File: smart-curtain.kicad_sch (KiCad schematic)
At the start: 71 parts, among them IC1 AS5040-ASST, IC2 ESP32-S3-MINI-1-N8, IC3 MPM3612GLQ-33-P, J1 USB4110-GF-A, J2 Limit, J3 Motor, J4 Qwiic 1, J5 Qwiic 2, SW1 Boot, SW2 Reset, U1 TMC2209-LA-T, U2 TPS25730DREFR

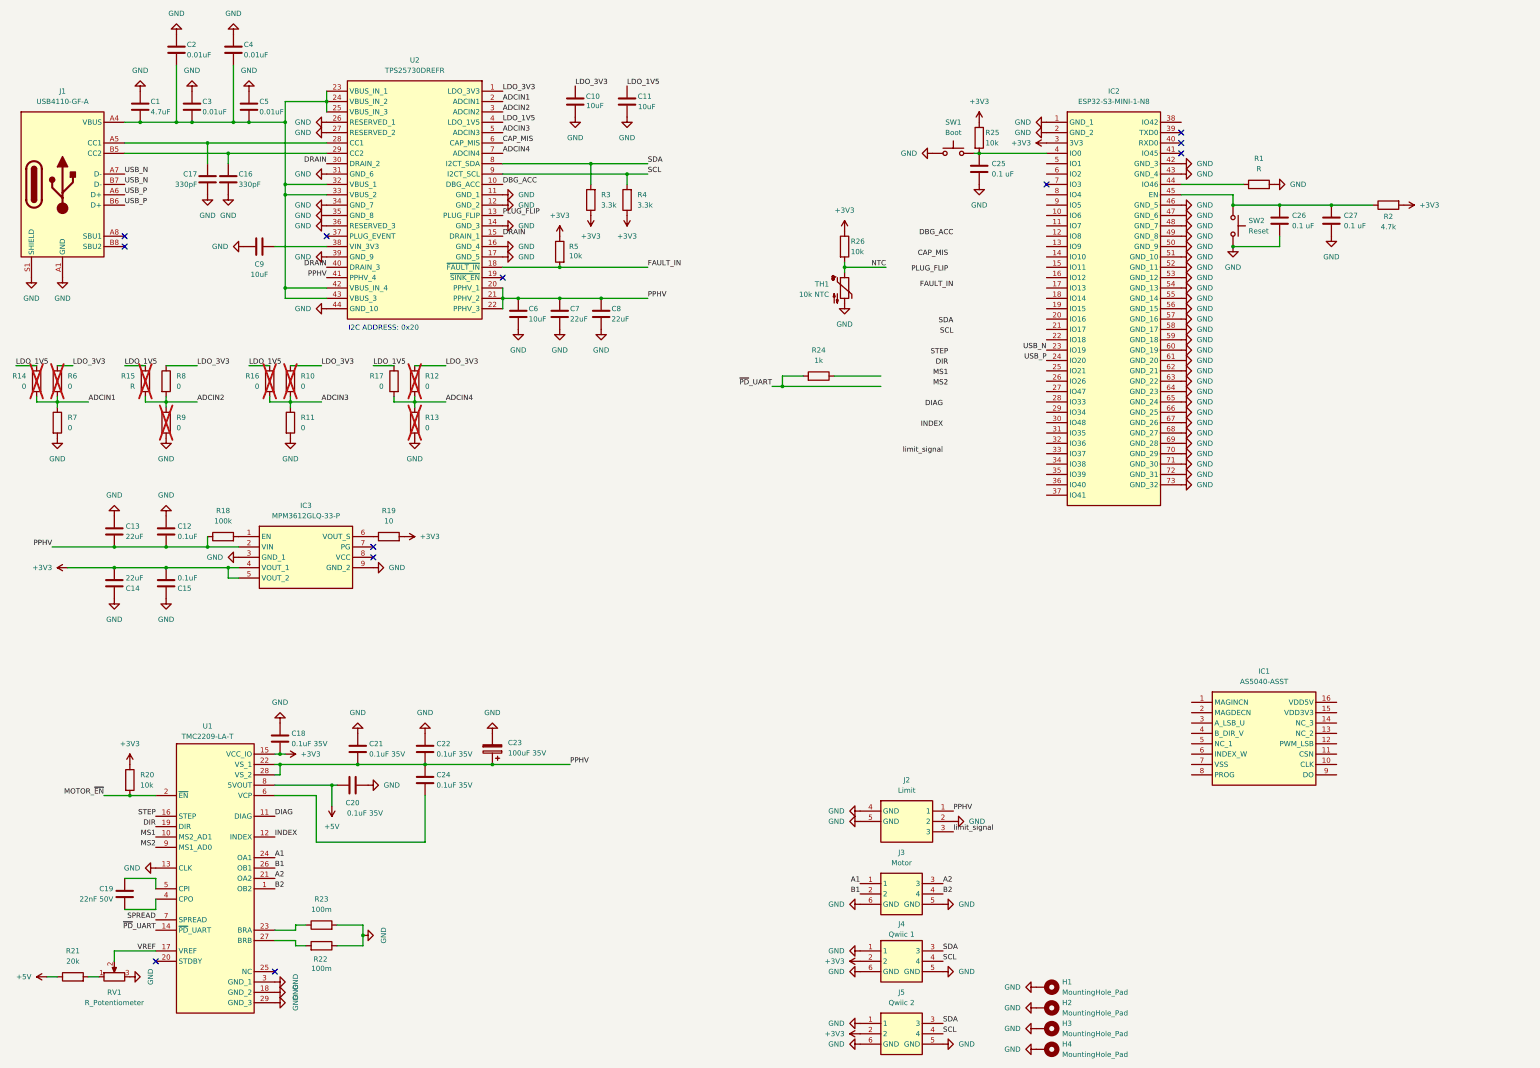
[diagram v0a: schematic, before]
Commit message: Update smart-curtain.kicad_sch
Connect labels to ESP pin`s
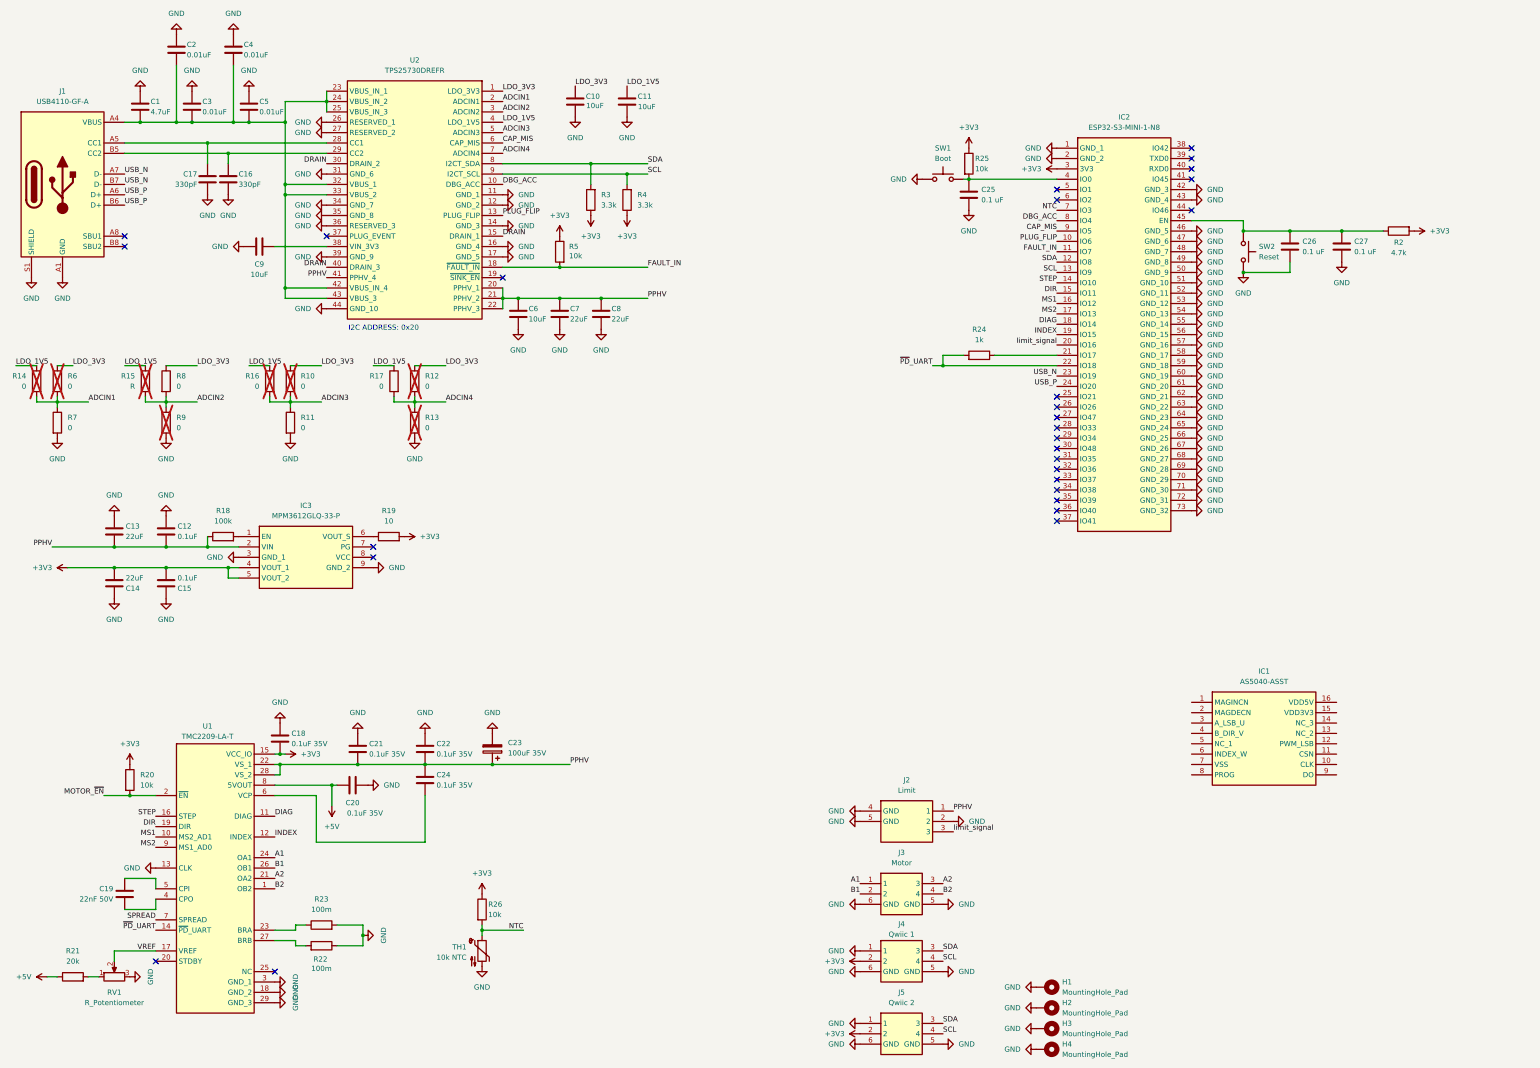
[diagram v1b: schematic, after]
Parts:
- removed R1: R, Resistor_SMD:R_0805_2012Metric, symbol Device:R
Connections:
- net CAP_MIS: now also IC2.9 (IO5)
- net DBG_ACC: now also IC2.8 (IO4)
- net DIAG: now also IC2.18 (IO14)
- net DIR: now also IC2.15 (IO11)
- net FAULT_IN: now also IC2.11 (IO7)
- net INDEX: now also IC2.19 (IO15)
- net MS1: now also IC2.16 (IO12)
- net MS2: now also IC2.17 (IO13)
- net NTC: now also IC2.7 (IO3)
- net PLUG_FLIP: now also IC2.10 (IO6)
- net SCL: now also IC2.13 (IO9)
- net SDA: now also IC2.12 (IO8)
- net STEP: now also IC2.14 (IO10)
- net limit_signal: now also IC2.20 (IO16)
- net ~{PD}_UART: now also IC2.22 (IO18)
- net at R24.1: now also IC2.21 (IO17)
- no-connect marks 12 -> 28
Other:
- moved on the sheet: C25, C26, C27, IC2, R2, R24, R25, R26, SW1, SW2, TH1

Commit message: Add AS5600
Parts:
- removed IC1: AS5040-ASST, Samacsys:SOP65P778X199-16N, symbol Samacsys:AS5040-ASST
- removed IC3: MPM3612GLQ-33-P, Samacsys:MPM3612GLQ33P, symbol Samacsys:MPM3612GLQ-33-P
- added C25: 100nF, symbol Device:C
- added U2: MPM3612GLQ-33-P, Samacsys:MPM3612GLQ33P, symbol Samacsys:MPM3612GLQ-33-P
- added U4: AS5600L, Samacsys:SOIC127P600X175-8N, symbol Samacsys:AS5600L
- renumbered C13 to C1, C16 to C10, C4 to C11, C5 to C12, C9 to C13, C18 to C14, C20 to C15, C21 to C16, C22 to C17, C24 to C18, C23 to C19, C14 to C2, C6 to C20, C7 to C21, C10 to C22, C8 to C23, C11 to C24, C25 to C26, C26 to C27, C27 to C28, C19 to C3, C1 to C4, C12 to C5, C15 to C6, C2 to C7, C3 to C8, C17 to C9, IC2 to IC1, R14 to R1, R16 to R10, R10 to R11, R11 to R12, R23 to R13, R22 to R14, R19 to R15, R17 to R16, R12 to R17, R13 to R18, R26 to R19, R6 to R2, R5 to R20, R3 to R21, R4 to R22, R25 to R23, R2 to R25, R7 to R3, R21 to R4, R20 to R5, R15 to R6, R8 to R7, R9 to R8, R18 to R9, U2 to U3
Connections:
- net +3V3: now also C25.1, U2.4 (VOUT_1), U2.5 (VOUT_2), U4.1 (VDD5V), U4.2 (VDD3V3)
- net GND: now also C25.2, U2.3 (GND_1), U2.9 (GND_2), U4.4 (GND)
- net PPHV: now also U2.2 (VIN)
- net SCL: now also U4.7 (SCL)
- net SDA: now also U4.6 (SDA)
- net at R9.2: now also U2.1 (EN)
- net at R15.1: now also U2.6 (VOUT_S)
- net AS5600_DIR: now reaches IC1.6 (IO2)
- net AS5600_DIR: now also U4.8 (DIR)
- no-connect marks 28 -> 29
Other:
- moved on the sheet: C26, C27, C28, IC1, R23, R24, R25, SW1, SW2

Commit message: Update smart-curtain.kicad_sch
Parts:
- added D1: LED Green, Diode_SMD:D_0402_1005Metric, symbol Device:LED
- added R26: 110, Resistor_SMD:R_0402_1005Metric, symbol Device:R
- C1, C10, C11, C12, C13, C14, C15, C16, C17, C18, C2, C20, C21, C22, C23, C24, C25, C26, C27, C28, C3, C4, C5, C6, C7, C8, C9: footprint (none) -> Capacitor_SMD:C_0402_1005Metric
- C19: footprint (none) -> Capacitor_SMD:CP_Elec_4x3
- R1, R10, R11, R12, R13, R14, R15, R16, R17, R18, R19, R2, R23, R24, R3, R4, R5, R6, R7, R8, R9: footprint (none) -> Resistor_SMD:R_0402_1005Metric
- R20, R21, R22, R25: footprint Resistor_SMD:R_0805_2012Metric -> Resistor_SMD:R_0402_1005Metric
- RV1: footprint (none) -> Potentiometer_SMD:Potentiometer_Bourns_3214W_Vertical
- SW1, SW2: footprint (none) -> Button_Switch_SMD:SW_Push_1P1T_NO_CK_KMR2
- TH1: footprint (none) -> Resistor_SMD:R_0402_1005Metric; B Parameter (none) -> 3435 K; Manufacturer_Part_Number (none) -> NTCG103JX103DTDS
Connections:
- net GND: now also D1.2 (A)
- net STATUS_LED: now reaches IC1.5 (IO1)
- net STATUS_LED: now also R26.2
- new net: D1.1 (K), R26.1
- no-connect marks 29 -> 28
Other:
- moved on the sheet: C1, C2, C5, C6, R15, R9, U2

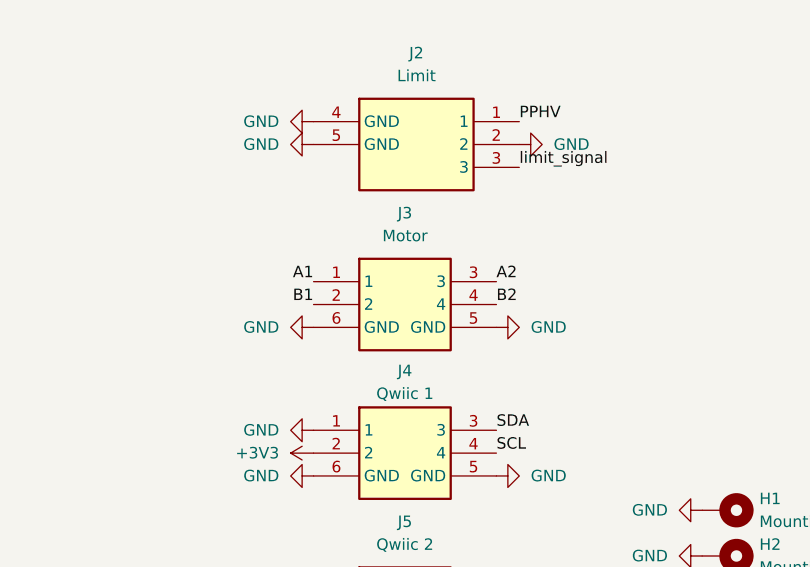
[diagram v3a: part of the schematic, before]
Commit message: swap B1 with A2
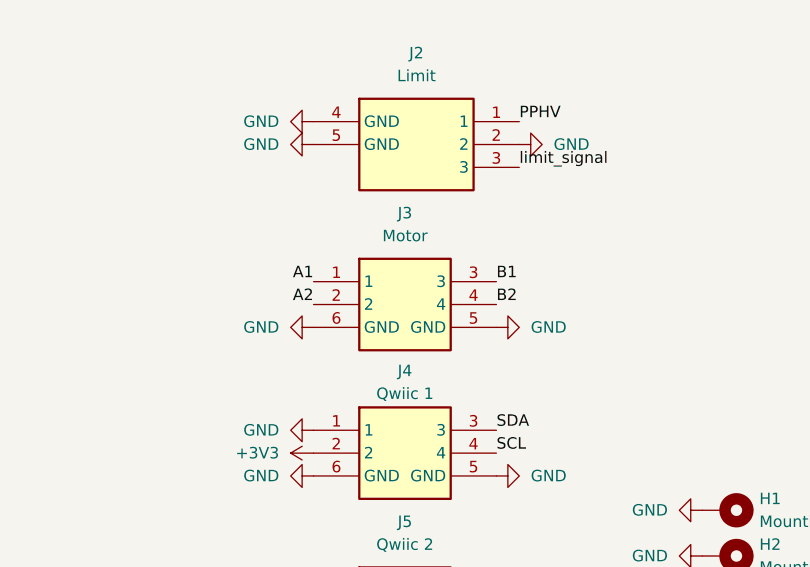
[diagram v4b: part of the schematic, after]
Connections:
- net A2: now also J3.2; no longer J3.3
- net B1: now also J3.3; no longer J3.2
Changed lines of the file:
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@@
 	)
 	(label "A2"
-		(at 250.19 236.22 0)
+		(at 229.87 238.76 180)
 		(effects
 			(font
 				(size 1.27 1.27)
 			)
-			(justify left bottom)
+			(justify right bottom)
 		)
 	)
@@
 	)
 	(label "B1"
-		(at 229.87 238.76 180)
+		(at 250.19 236.22 0)
 		(effects
 			(font
 				(size 1.27 1.27)
 			)
-			(justify right bottom)
+			(justify left bottom)
 		)
 	)
